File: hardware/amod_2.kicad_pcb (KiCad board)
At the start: 4 copper layers, 100 x 100 mm, 234 parts, among them J1001 SMA, J1002 SMA, J1003 SMA, J1004 SMA, J101 USB-C, J201 SMA, J202 SMA, J301 SMA, J302 SMA, J303 SMA, J304 SMA, J401 SMA, J402 VM in, J403 coil, J501 SMA, J502 SMA, J503 SMA, J504 SMA, J505 Pmod, J601 SMA, J602 SMA, J701 SMA, J702 SMA, J703 SMA, J704 SMA, J801 SMA, J802 SMA, J803 SMA, J804 SMA, J901 SMA, Q1001 AO3401A, Q1002 2N7002, Q1003 AO3401A, Q1004 AO3400A, Q301 AO3401A, Q401 AO3401A, Q501 AO3401A, Q601 AO3401A, Q701 AO3401A, Q801 AO3401A, Q901 AO3401A, Q902 MMBT3904, SW1001 ON, SW301 ON, SW401 ON, SW501 ON, SW601 ON, SW701 ON, SW801 ON, SW802 DIP4, SW901 ON, U1001 OPA810, U1002 OPA810, U101 TPS65131, U102 LM2664, U201 THS3491, U301 OPA847, U401 DRV8876, U402 OPA810, U501 LMH6629, U502 LMH6629, U601 OPA810, U701 OPA810, U702 OPA810, U901 TPS22917, U902 LMH6629

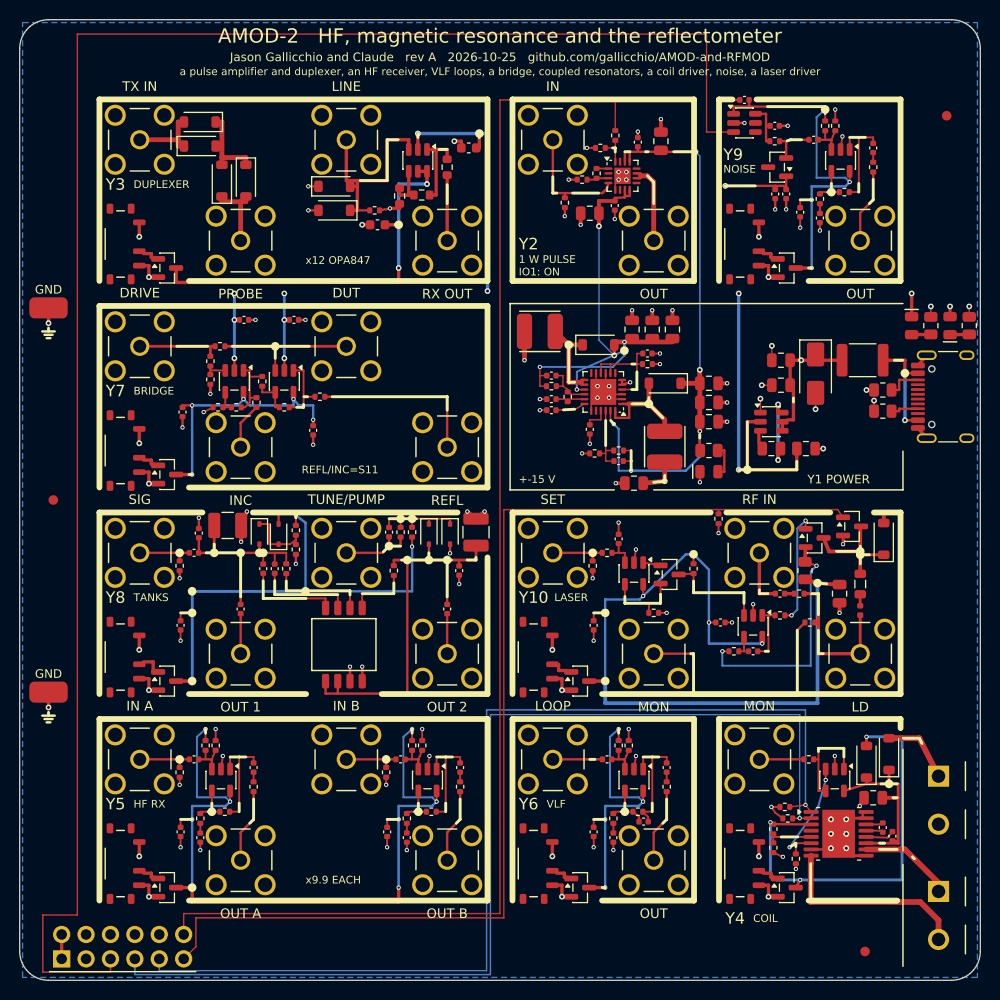
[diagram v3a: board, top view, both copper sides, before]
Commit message: Silkscreen says what each tile is and whose jack is whose: jack names on their own tile's frame, titles in words on the top frame, ranges and levels placed inside; tutorial section numbers off the boards; README tables of every tile (what, chip link, specs, limits, experiments, use, what to buy) and handbook entries as tables with a picture of each tile, both from boards/tile_docs.py
Co-Authored-By: Claude Opus 5.5 <noreply@anthropic.com>
Claude-Session: https://claude.ai/code/session_01RKeoKvFFzjk3cEBLCXXHnB
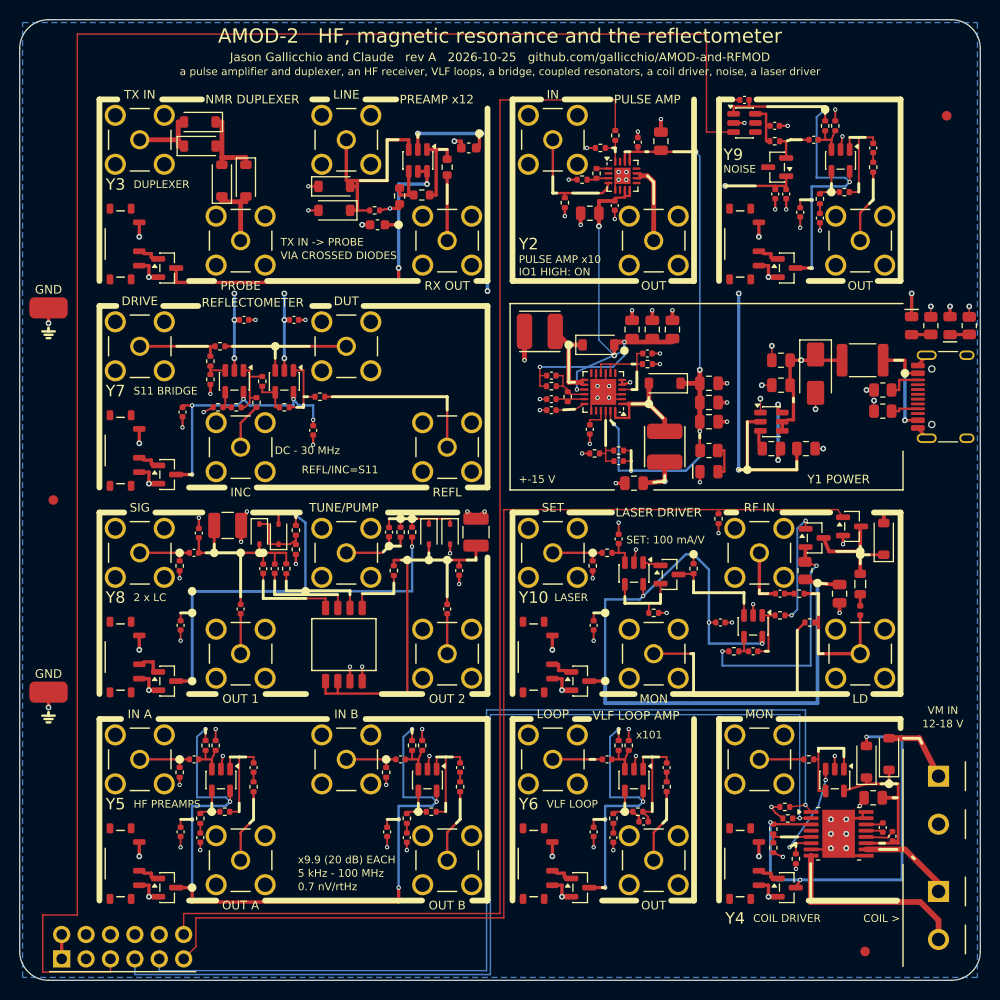
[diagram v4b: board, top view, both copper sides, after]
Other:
- board text added: "0.7 nV/rtHz"
- board text added: "12-18 V"
- board text added: "2 x LC"
- board text added: "5 kHz - 100 MHz"
- board text added: "COIL >"
- board text added: "COIL DRIVER"
- board text added: "DC - 30 MHz"
- board text added: "HF PREAMPS"
- board text added: "IO1 HIGH: ON"
- board text added: "LASER DRIVER"
- board text added: "NMR DUPLEXER"
- board text added: "PREAMP x12"
- board text added: "PULSE AMP"
- board text added: "PULSE AMP x10"
- board text added: "REFLECTOMETER"
- board text added: "S11 BRIDGE"
- board text added: "SET: 100 mA/V"
- board text added: "TX IN -> PROBE"
- board text added: "VIA CROSSED DIODES"
- board text added: "VLF LOOP"
- board text added: "VLF LOOP AMP"
- board text added: "VM IN"
- board text added: "x101"
- board text added: "x9.9 (20 dB) EACH"
- board text removed: "1 W PULSE"
- board text removed: "BRIDGE"
- board text removed: "COIL"
- board text removed: "HF RX"
- board text removed: "IO1: ON"
- board text removed: "TANKS"
- board text removed: "VLF"
- board text removed: "x12 OPA847"
- board text removed: "x9.9 EACH"
